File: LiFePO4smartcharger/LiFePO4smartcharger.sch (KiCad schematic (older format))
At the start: 104 parts, among them J1 Conn_01x02, J10 Conn_01x01, J11 Conn_01x01, J12 Conn_01x04, J14 Conn_01x02, J2 Conn_02x03_Odd_Even, J3 Conn_01x02, J4 Conn_01x02, J5 Conn_01x02, J6 Conn_01x01, J7 Conn_01x01, J8 Conn_01x02, J9 Conn_01x02, Q1 TIP42, Q2 TIP41, Q3 2N3906, Q4 TIP41C, U1 ATMEGA328P-PU, U2 LM358, U3 LCD-016N002L, U4 TL494, U9 LM7805_TO220, X3 16MHz

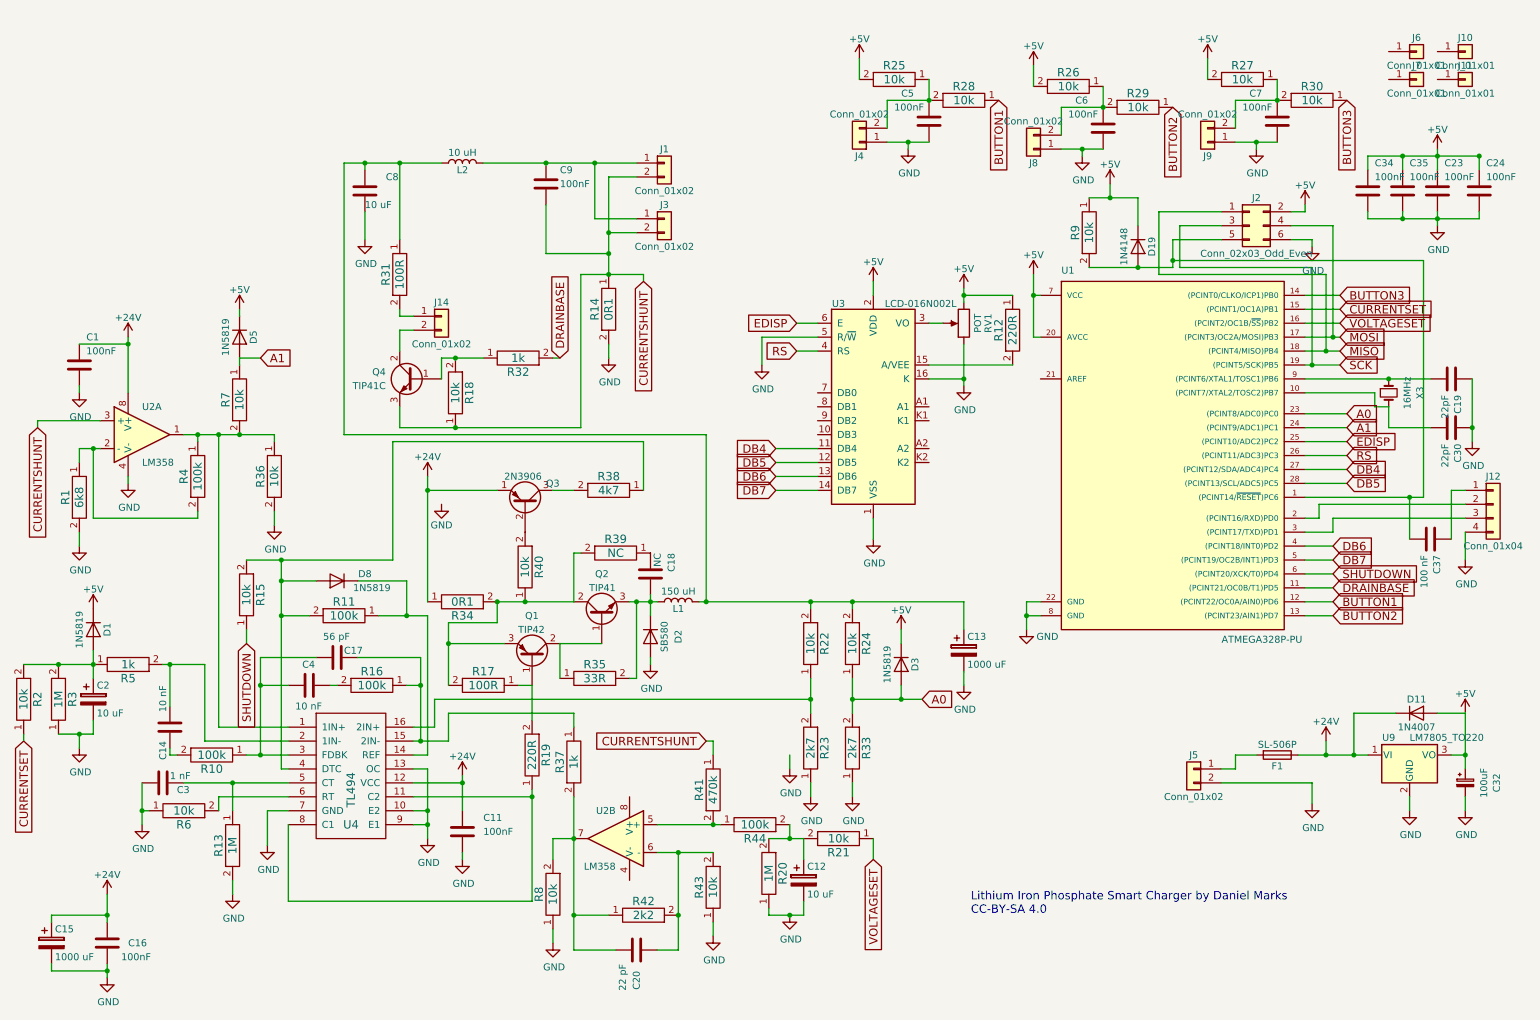
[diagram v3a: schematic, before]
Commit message: Removed on-board RF filter inductor
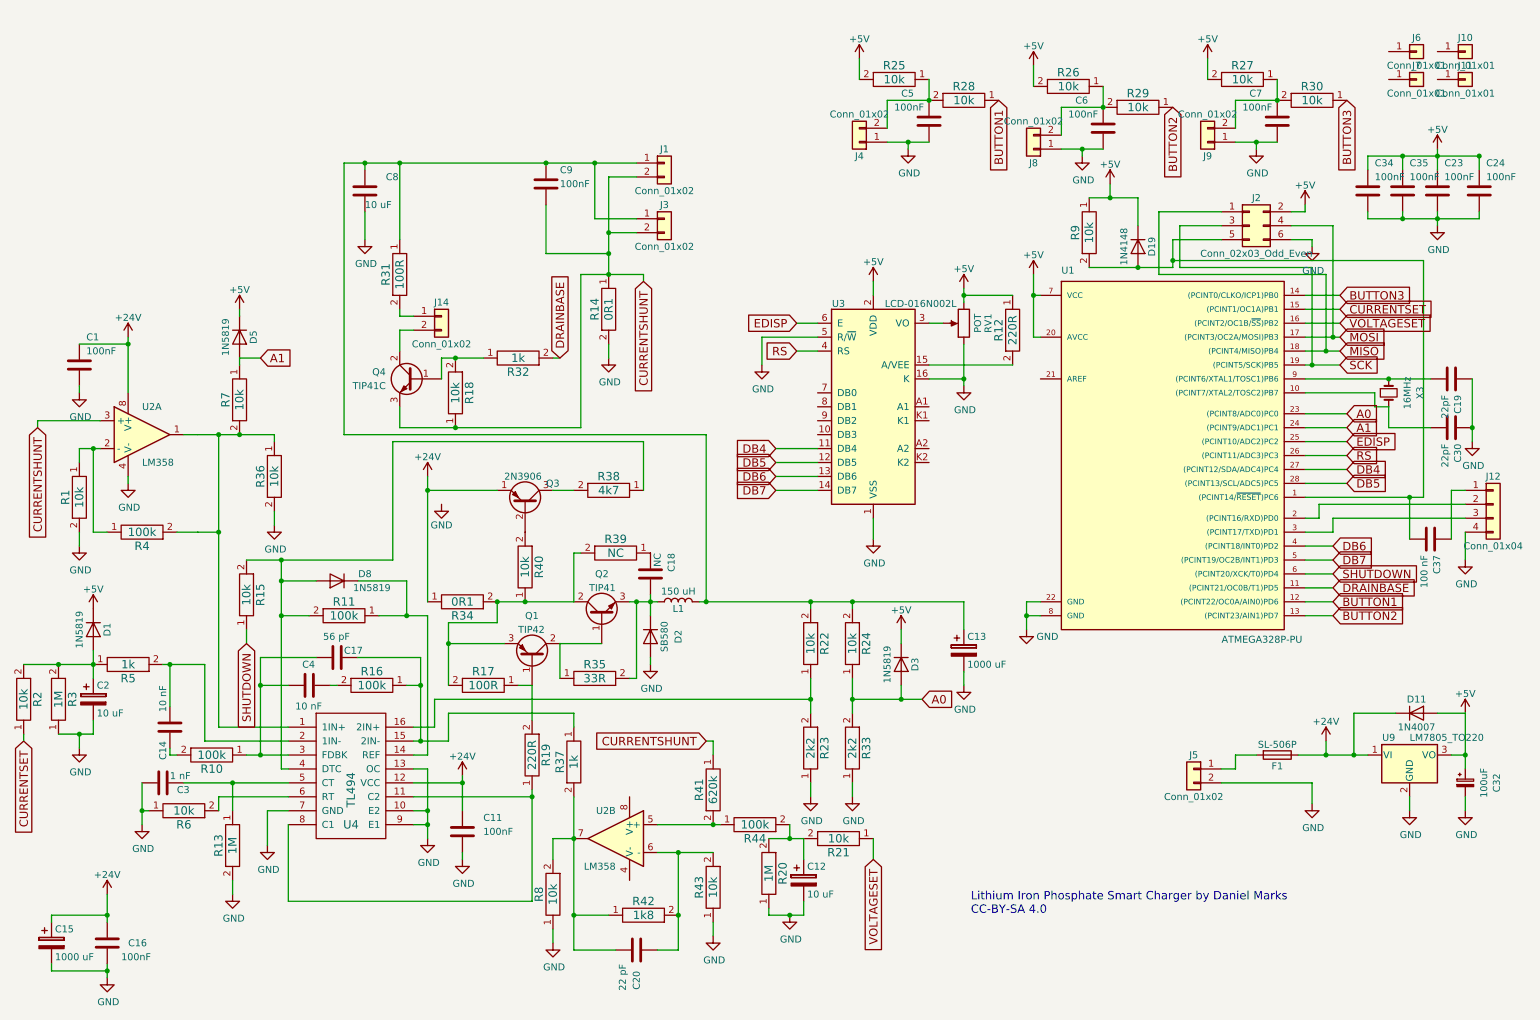
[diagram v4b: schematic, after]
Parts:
- removed L2: 10 uH, Inductors_THT:L_Radial_D14.2mm_P10.00mm_Neosid_SD14, symbol L
- R1: value 6k8 -> 10k
- R23, R33: value 2k7 -> 2k2
- R41: value 470k -> 620k
- R42: value 2k2 -> 1k8
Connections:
- net at C9.1, J1.1 (Pin_1), J3.1 (Pin_1): now also C13.1, C8.1, L1.2, R22.2, R24.2, R31.1
- net at R36.1, R7.2, U2.1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: now also R4.2; no longer R4.1
- net at R1.1, U2.2 (-): now also R4.1; no longer R4.2
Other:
- moved on the sheet: R4

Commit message: Added spot for LM35 temperature sensor
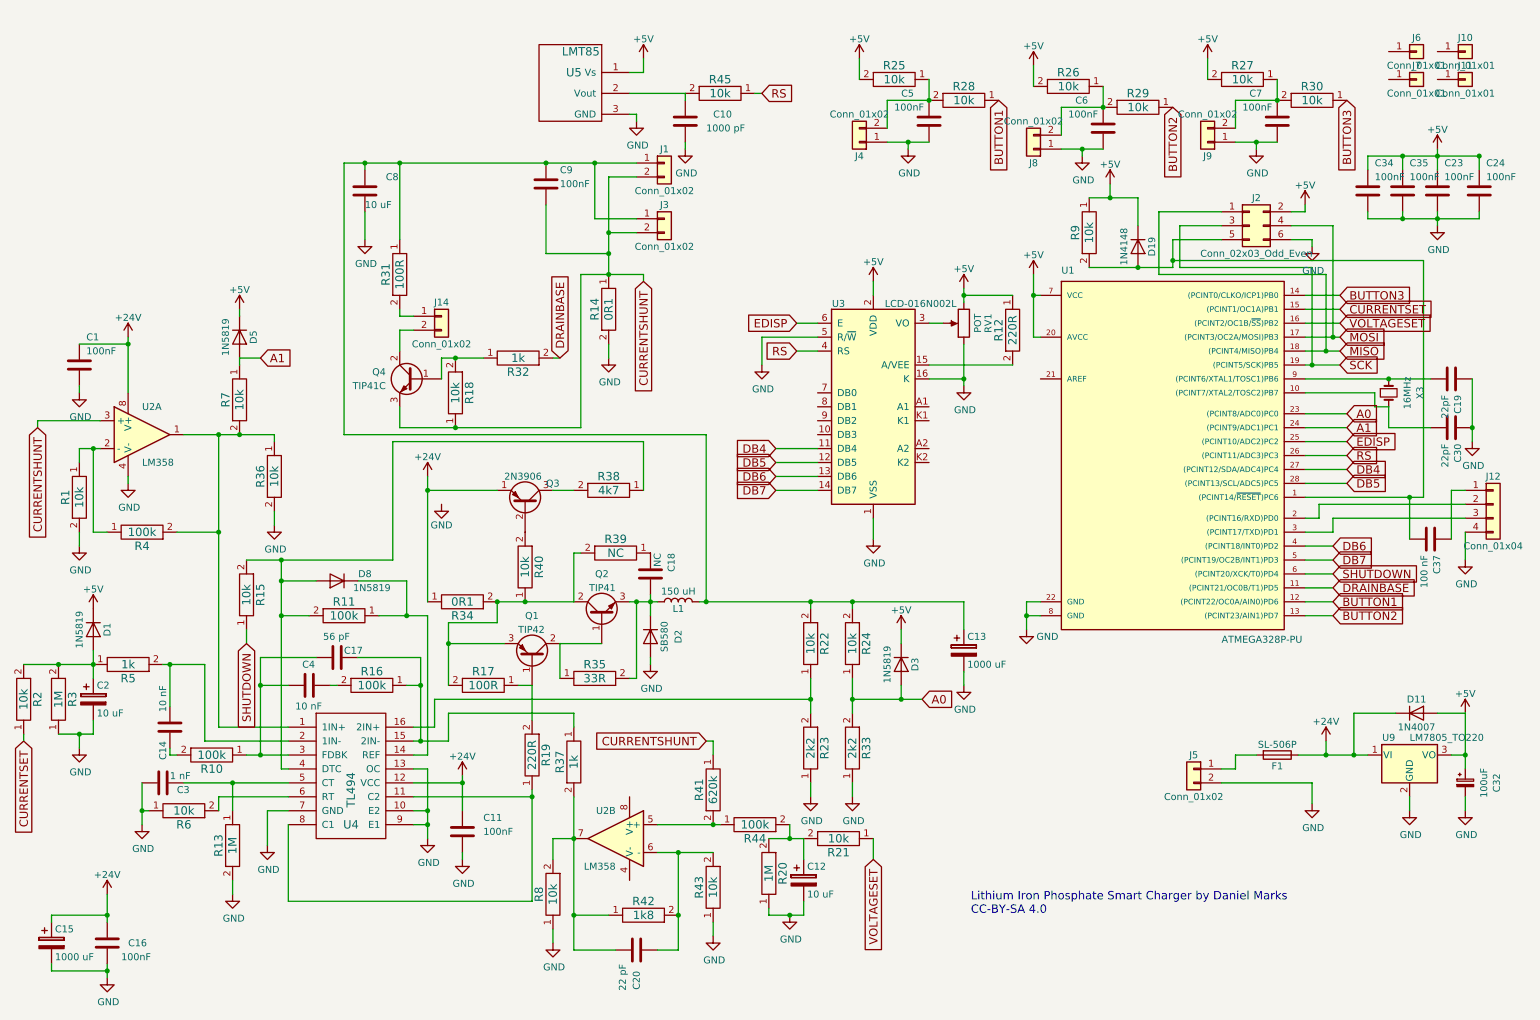
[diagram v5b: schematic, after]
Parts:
- added C10: 1000 pF, Capacitors_THT:C_Disc_D5.0mm_W2.5mm_P5.00mm, symbol C
- added R45: 10k, Resistors_THT:R_Axial_DIN0207_L6.3mm_D2.5mm_P7.62mm_Horizontal, symbol RES
- added U5: LMT85, TO_SOT_Packages_THT:TO-92_Inline_Wide, symbol LM35
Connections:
- net +5V: now also U5.1 (Vs)
- net GND: now also C10.2, U5.3 (GND)
- net RS: now also R45.1
- new net: C10.1, R45.2, U5.2 (Vout)
